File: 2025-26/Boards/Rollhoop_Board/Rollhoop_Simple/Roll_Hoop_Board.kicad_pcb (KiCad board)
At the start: 2 copper layers, 106.7 x 36 mm, 29 parts, among them J1 DTM13-12PA, J2 DTM13-12PA, J3 Conn_01x04_Pin, J4 043045-0612, J5 043045-0612, Q1 AO3401A, Q2 AO3400A, Q3 AO3400A, Q4 AO3400A, U2 SN65HVD230, U3 STM32C011F4Px, U4 UA78M33QDCYRQ1

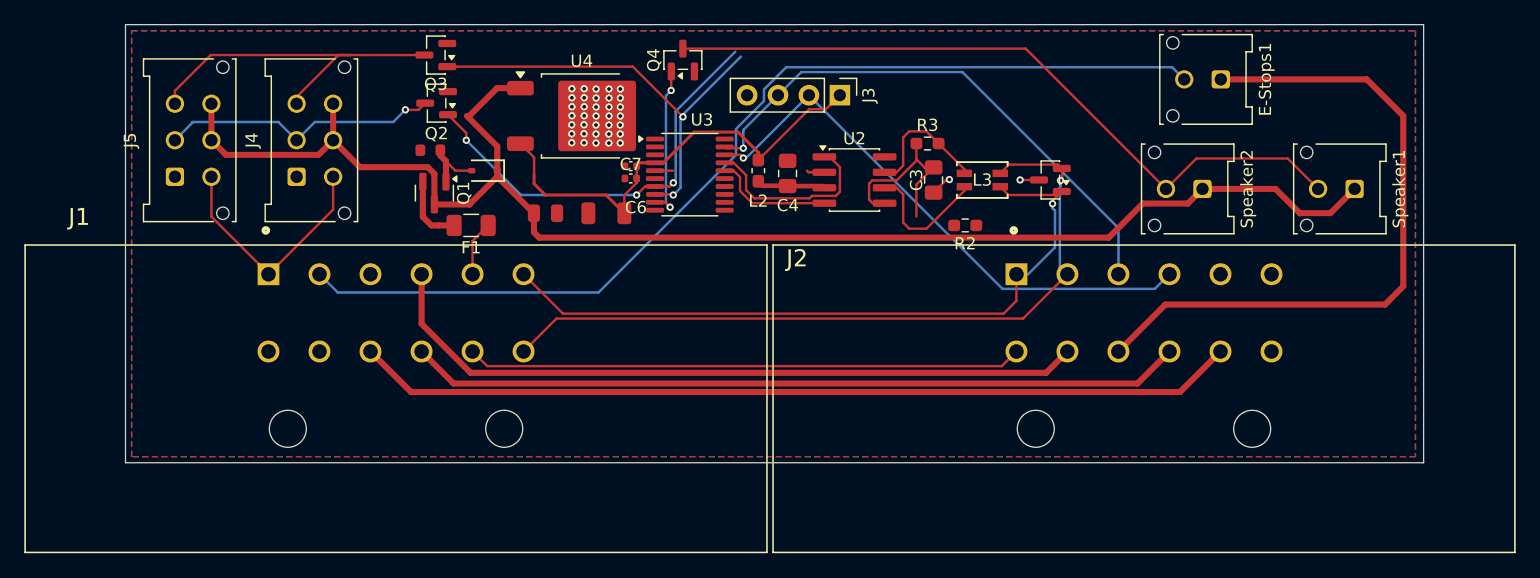
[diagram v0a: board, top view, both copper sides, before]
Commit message: Simple Rollhoop update
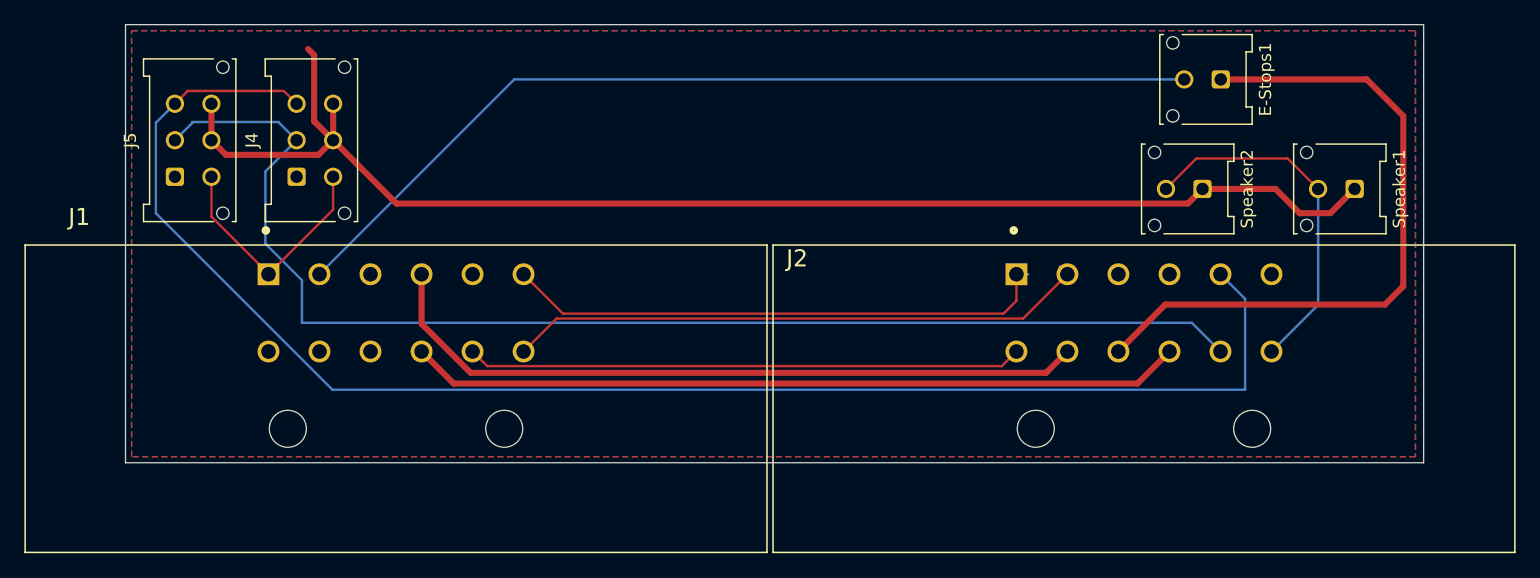
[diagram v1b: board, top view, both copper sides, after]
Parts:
- removed C1: 10uF, PCM_JLCPCB:C_0805
- removed C2: 22uF, PCM_JLCPCB:C_1206
- removed C3: 4.7nF, Capacitor_SMD:C_0805_2012Metric_Pad1.18x1.45mm_HandSolder
- removed C4: 10uF, Capacitor_SMD:C_0805_2012Metric_Pad1.18x1.45mm_HandSolder
- removed C6: 100nF, Capacitor_SMD:C_0402_1005Metric
- removed C7: 4.7μF, Capacitor_SMD:C_0402_1005Metric
- removed D1: BZT52C10S, PCM_JLCPCB:D_SOD-323
- removed D2: ESD2CANFD24DBZRQ1, Package_TO_SOT_SMD:SOT-23
- removed F1: Fuse, Fuse:Fuse_1206_3216Metric
- removed J3: Conn_01x04_Pin, Connector_PinHeader_2.54mm:PinHeader_1x04_P2.54mm_Vertical
- removed L2: GZ1608D601TF, Inductor_SMD:L_0603_1608Metric_Pad1.05x0.95mm_HandSolder
- removed L3: ACT1210-101-2P-TL00, RLH_BOARD:IND_01-2P-TL00_TDK
- removed Q1: AO3401A, Package_TO_SOT_SMD:SOT-23
- removed Q2, Q3, Q4: AO3400A, Package_TO_SOT_SMD:SOT-23
- removed R1: 13kΩ, PCM_JLCPCB:R_0603
- removed R2, R3: 60, Resistor_SMD:R_0603_1608Metric_Pad0.98x0.95mm_HandSolder
- removed U2: SN65HVD230, Package_SO:SOIC-8_3.9x4.9mm_P1.27mm
- removed U3: STM32C011F4Px, Package_SO:TSSOP-20_4.4x6.5mm_P0.65mm
- removed U4: UA78M33QDCYRQ1, Package_TO_SOT_SMD:TO-252-2
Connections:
- net DSH_CAN_H renamed CAN_H
- net DSH_CAN_L renamed CAN_L
- net DSH_CAN_S renamed CAN_S
- J2 pad 5: unconnected-(J2-Pad5) -> Red_Out
- J2 pad 7: unconnected-(J2-Pad7) -> Speaker_Out
- J2 pad 8: Extra -> Green_Out
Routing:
- net Red_Out: track 29.2 -> 126.9 mm
- net Green_Out: track 23.1 -> 105.0 mm, vias 1 -> 0
- net Extra: track 72.6 -> 0.00 mm
- net SWDIO: track 45.9 -> 0.00 mm, vias 1 -> 0
- net SWCLK: track 45.6 -> 0.63 mm, vias 1 -> 0
- net RLH_3.3V: track 38.2 -> 0.00 mm
- net Red_LED: track 36.3 -> 0.00 mm, vias 2 -> 0
- net Green_LED: track 34.9 -> 0.00 mm, vias 3 -> 0
- net Speaker_Out: track 59.0 -> 29.5 mm
- net TX: track 15.3 -> 0.00 mm
- net Vref: track 15.1 -> 0.00 mm
- net CAN_H: track 61.9 -> 48.2 mm, vias 1 -> 0
- net CAN_L: track 59.0 -> 45.4 mm, vias 1 -> 0
- net Speaker: track 12.9 -> 0.00 mm, vias 2 -> 0
- net Net-(U2-CANL): track 10.9 -> 0.00 mm
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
